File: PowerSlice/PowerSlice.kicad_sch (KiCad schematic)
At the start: 25 parts, among them J1 Conn_01x08_Pin, J2 Barrel_Jack, J3 Screw_Terminal_01x02, SW1 SW_ESTOP, U1 PTH08080WAD, U2 PTH08080WAD, U3 INA214BIDCKR, U4 INA214BIDCKR, U5 INA214BIDCKR, U6 NUCLEO-F303K8

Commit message: Update PowerSlice.kicad_sch
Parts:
- added C8: 0.1uF, symbol Device:C
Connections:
- net +3V3: now also U6.4_1 (VIN), C8.2
- net GND: now also U6.3_4 (GND_1), U6.4_2 (GND_2), C8.1
- net R1_Current: now also U6.4_10 (PA3)
- net R2_Current: now also U6.4_11 (PA1)
- net R3_Current: now also U6.4_12 (PA0)
- net SCL: now also U6.3_8 (PB6)
- net SDA: now also U6.3_7 (PB7)

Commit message: finished preliminary schematic
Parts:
- removed C8: 0.1uF, symbol Device:C
- added C8: 0.1uF, symbol Device:C_Small
- added R10, R11, R12, R9: 100k, symbol Device:R
- added R6, R7, R8: 330k, symbol Device:R
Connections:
- net +3V3: now also R12.1; no longer U6.4_1 (VIN)
- net +5V: now also U6.4_4 (+5V), C8.2
- net 12V_L: now also R6.1
- net 3V3_L: now also R8.1
- net 5V_L: now also R7.1
- net GND: now also C8.1, R10.2, R11.2, R9.2
- net LED: now also U6.4_6 (PA7)
- net R1_Current: now also U6.4_12 (PA0); no longer U6.4_10 (PA3)
- net R3_Current: now also U6.4_10 (PA3); no longer U6.4_12 (PA0)
- net RESET: now also U6.3_3 (NRST_1), R12.2
- net 12VSns: now reaches U6.4_7 (PA6)
- net 12VSns: now also R6.2, R9.1
- net 5VSns: now reaches U6.4_8 (PA5)
- net 5VSns: now also R10.1, R7.2
- net 3V3Sns: now reaches U6.4_9 (PA4)
- net 3V3Sns: now also R11.1, R8.2
- no-connect marks 2 -> 18

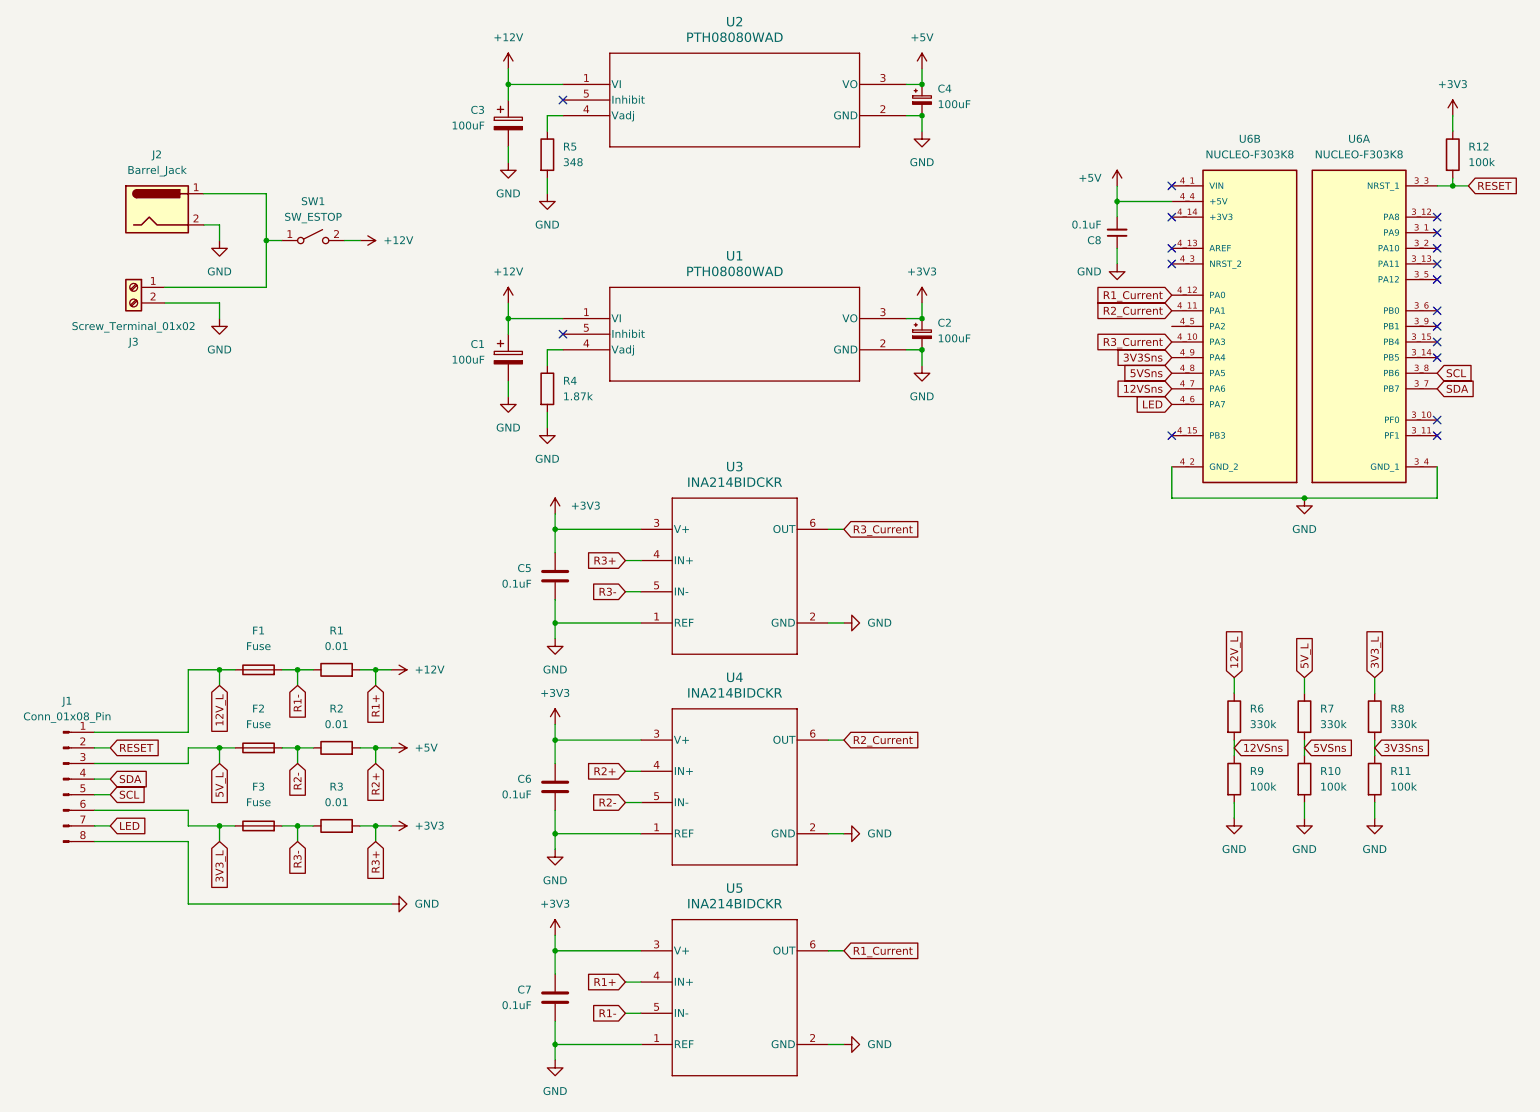
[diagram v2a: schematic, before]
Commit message: fixed all ERC warnings/errors
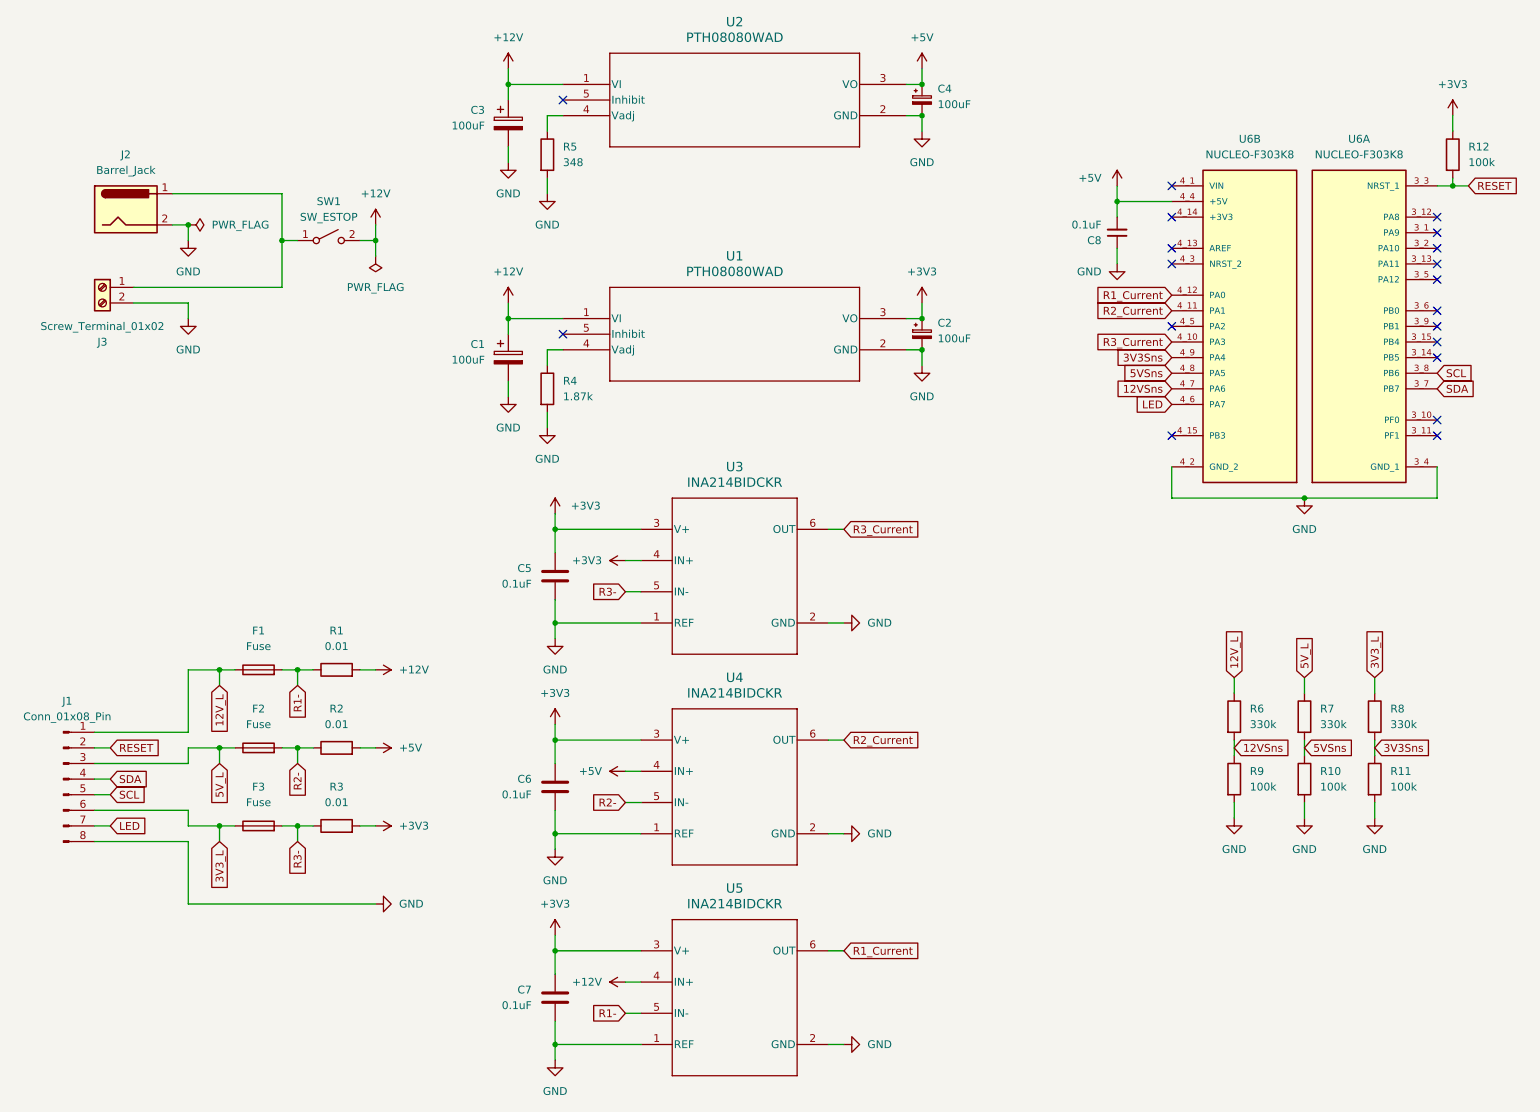
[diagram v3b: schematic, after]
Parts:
- U1, U2: footprint EUF5 -> PTH08080WAD:EUF5
- U3, U4, U5: footprint DCK0006A_N -> INA214BIDCKR:DCK0006A_N
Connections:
- no-connect marks 18 -> 19
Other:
- moved on the sheet: J2, J3, SW1

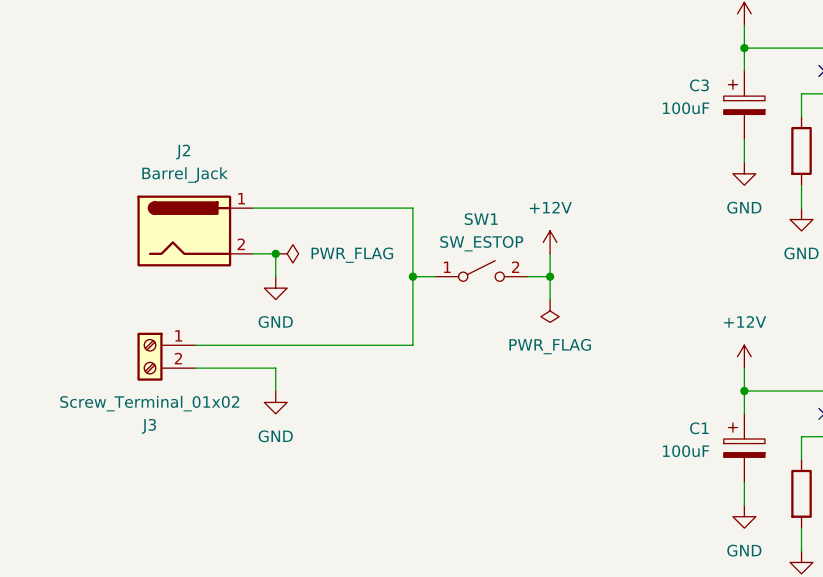
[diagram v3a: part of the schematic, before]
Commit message: updated some small pieces, namely estop is changed from a button symbol to a screw terminal for external connection
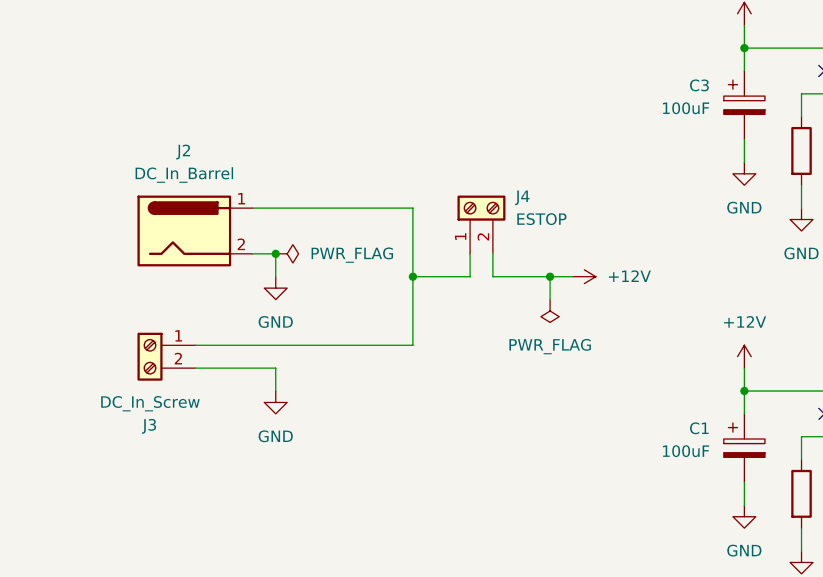
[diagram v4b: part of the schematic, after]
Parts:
- removed SW1: SW_ESTOP, symbol Switch:SW_SPST
- added J4: ESTOP, symbol Connector:Screw_Terminal_01x02
- J2: value Barrel_Jack -> DC_In_Barrel
- J3: value Screw_Terminal_01x02 -> DC_In_Screw
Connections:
- net +12V: now also J4.2 (Pin_2)
- net at J2.1, J3.1 (Pin_1): now also J4.1 (Pin_1)
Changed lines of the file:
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@@
 	(wire
 		(pts
-			(xy 72.39 52.07) (xy 74.93 52.07)
-		)
-		(stroke
-			(width 0)
-			(type default)
-		)
-	)
-	(wire
-		(pts
 			(xy 96.52 36.83) (xy 96.52 39.37)
 		)
@@
 	(wire
 		(pts
+			(xy 68.58 49.53) (xy 68.58 52.07)
+		)
+		(stroke
+			(width 0)
+			(type default)
+		)
+	)
+	(wire
+		(pts
 			(xy 72.39 121.92) (xy 74.93 121.92)
 		)
@@
 	(wire
 		(pts
+			(xy 68.58 52.07) (xy 74.93 52.07)
+		)
+		(stroke
+			(width 0)
+			(type default)
+		)
+	)
+	(wire
+		(pts
 			(xy 62.23 134.62) (xy 64.77 134.62)
 		)
@@
 	(wire
 		(pts
+			(xy 77.47 52.07) (xy 74.93 52.07)
+		)
+		(stroke
+			(width 0)
+			(type default)
+		)
+	)
+	(wire
+		(pts
 			(xy 52.07 121.92) (xy 49.53 121.92)
 		)
@@
 	(wire
 		(pts
-			(xy 74.93 49.53) (xy 74.93 52.07)
-		)
-		(stroke
-			(width 0)
-			(type default)
-		)
-	)
-	(wire
-		(pts
 			(xy 237.49 133.35) (xy 237.49 135.89)
 		)
@@
 	(wire
 		(pts
-			(xy 59.69 52.07) (xy 62.23 52.07)
+			(xy 59.69 52.07) (xy 66.04 52.07)
 		)
 		(stroke
@@
 	(wire
 		(pts
+			(xy 66.04 49.53) (xy 66.04 52.07)
+		)
+		(stroke
+			(width 0)
+			(type default)
+		)
+	)
+	(wire
+		(pts
 			(xy 49.53 147.32) (xy 49.53 149.86)
 		)
@@
 			)
 		)
-		(property "Value" "Screw_Terminal_01x02"
+		(property "Value" "DC_In_Screw"
 			(at 30.48 66.04 0)
 			(effects
@@
 	)
 	(symbol
+		(lib_id "Connector:Screw_Terminal_01x02")
+		(at 66.04 44.45 90)
+		(unit 1)
+		(exclude_from_sim no)
+		(in_bom yes)
+		(on_board yes)
+		(dnp no)
+		(fields_autoplaced yes)
+		(property "Reference" "J4"
+			(at 71.12 43.1799 90)
+			(effects
+				(font
+					(size 1.27 1.27)
+				)
+				(justify right)
+			)
+		)
+		(property "Value" "ESTOP"
+			(at 71.12 45.7199 90)
+			(effects
+				(font
+					(size 1.27 1.27)
+				)
+				(justify right)
+			)
+		)
+		(property "Footprint" ""
+			(at 66.04 44.45 0)
+			(effects
+				(font
+					(size 1.27 1.27)
+				)
+				(hide yes)
+			)
+		)
+		(property "Datasheet" "~"
+			(at 66.04 44.45 0)
+			(effects
+				(font
+					(size 1.27 1.27)
+				)
+				(hide yes)
+			)
+		)
+		(property "Description" "Generic screw terminal, single row, 01x02, script generated (kicad-library-utils/schlib/autogen/connector/)"
+			(at 66.04 44.45 0)
+			(effects
+				(font
+					(size 1.27 1.27)
+				)
+				(hide yes)
+			)
+		)
+		(pin "2"
+		)
+		(pin "1"
+		)
+		(instances
+			(project ""
+				(path "/871cf238-4ac7-4d02-abe8-ea643d22c598"
+					(reference "J4")
+					(unit 1)
+				)
+			)
+		)
+	)
+	(symbol
 		(lib_id "Device:R")
 		(at 102.87 38.1 0)
@@
 	(symbol
 		(lib_id "power:+12V")
-		(at 74.93 49.53 0)
+		(at 77.47 52.07 270)
 		(unit 1)
 		(exclude_from_sim no)
@@
 		(fields_autoplaced yes)
 		(property "Reference" "#PWR03"
-			(at 74.93 53.34 0)
+			(at 73.66 52.07 0)
 			(effects
 				(font
@@
 		)
 		(property "Value" "+12V"
-			(at 74.93 44.45 0)
+			(at 81.28 52.0699 90)
 			(effects
 				(font
 					(size 1.27 1.27)
 				)
+				(justify left)
 			)
 		)
 		(property "Footprint" ""
-			(at 74.93 49.53 0)
+			(at 77.47 52.07 0)
 			(effects
 				(font
@@
 		)
 		(property "Datasheet" ""
-			(at 74.93 49.53 0)
+			(at 77.47 52.07 0)
 			(effects
 				(font
@@
 		)
 		(property "Description" "Power symbol creates a global label with name \"+12V\""
-			(at 74.93 49.53 0)
+			(at 77.47 52.07 0)
 			(effects
 				(font
@@
 	)
 	(symbol
-		(lib_id "Switch:SW_SPST")
-		(at 67.31 52.07 0)
-		(unit 1)
-		(exclude_from_sim no)
-		(in_bom yes)
-		(on_board yes)
-		(dnp no)
-		(fields_autoplaced yes)
-		(property "Reference" "SW1"
-			(at 67.31 45.72 0)
-			(effects
-				(font
-					(size 1.27 1.27)
-				)
-			)
-		)
-		(property "Value" "SW_ESTOP"
-			(at 67.31 48.26 0)
-			(effects
-				(font
-					(size 1.27 1.27)
-				)
-			)
-		)
-		(property "Footprint" ""
-			(at 67.31 52.07 0)
-			(effects
-				(font
-					(size 1.27 1.27)
-				)
-				(hide yes)
-			)
-		)
-		(property "Datasheet" "~"
-			(at 67.31 52.07 0)
-			(effects
-				(font
-					(size 1.27 1.27)
-				)
-				(hide yes)
-			)
-		)
-		(property "Description" "Single Pole Single Throw (SPST) switch"
-			(at 67.31 52.07 0)
-			(effects
-				(font
-					(size 1.27 1.27)
-				)
-				(hide yes)
-			)
-		)
-		(pin "2"
-		)
-		(pin "1"
-		)
-		(instances
-			(project ""
-				(path "/871cf238-4ac7-4d02-abe8-ea643d22c598"
-					(reference "SW1")
-					(unit 1)
-				)
-			)
-		)
-	)
-	(symbol
 		(lib_id "Device:C_Polarized")
 		(at 96.52 71.12 0)
@@
 			)
 		)
-		(property "Value" "Barrel_Jack"
+		(property "Value" "DC_In_Barrel"
 			(at 34.29 40.64 0)
 			(effects
